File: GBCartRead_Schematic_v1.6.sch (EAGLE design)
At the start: 32 parts, among them IC1 74LS595N, IC2 74LS595N

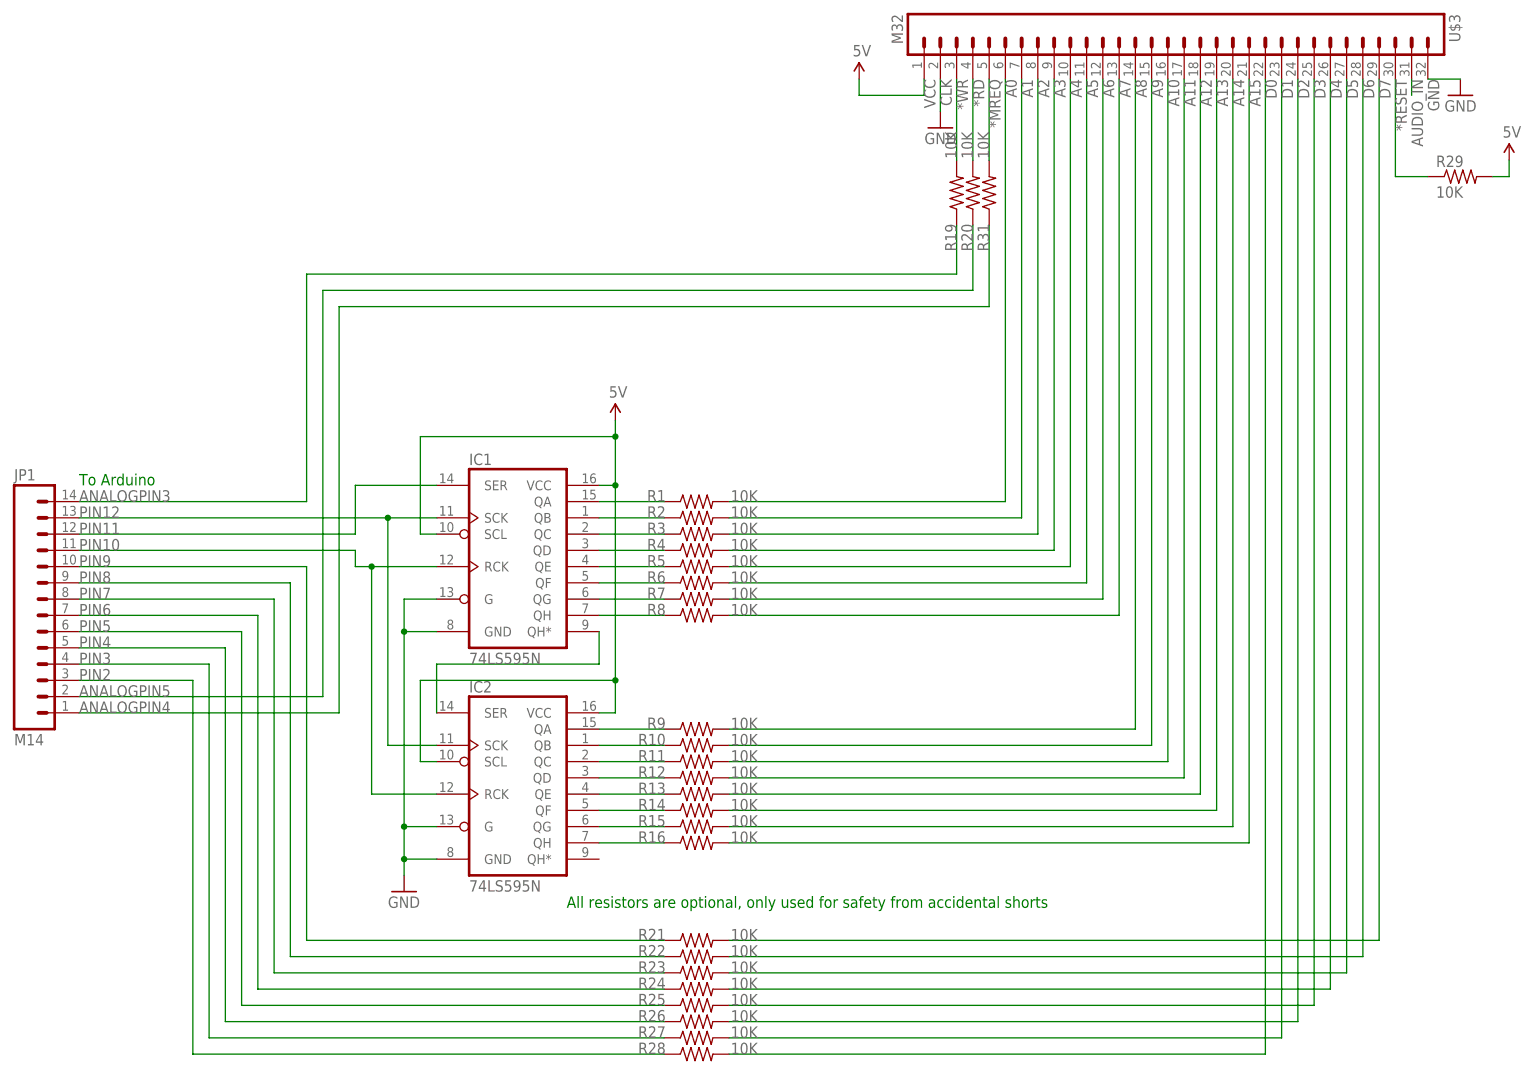
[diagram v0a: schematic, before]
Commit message: v1.6 (3 January 2015) - Speed increase by using a higher baud rate (400Kbit from 57.6Kbit) and using hardware SPI (thanks David R) - Changed SCK from pin 12 to pin 13 for SPI - RAM writing speed increase by continually sending 64bytes data from PC and pausing for 5 ms in-between (Compatible with Gameboy Cart Shield v1.2 if you connect pins 12 and 13 together)
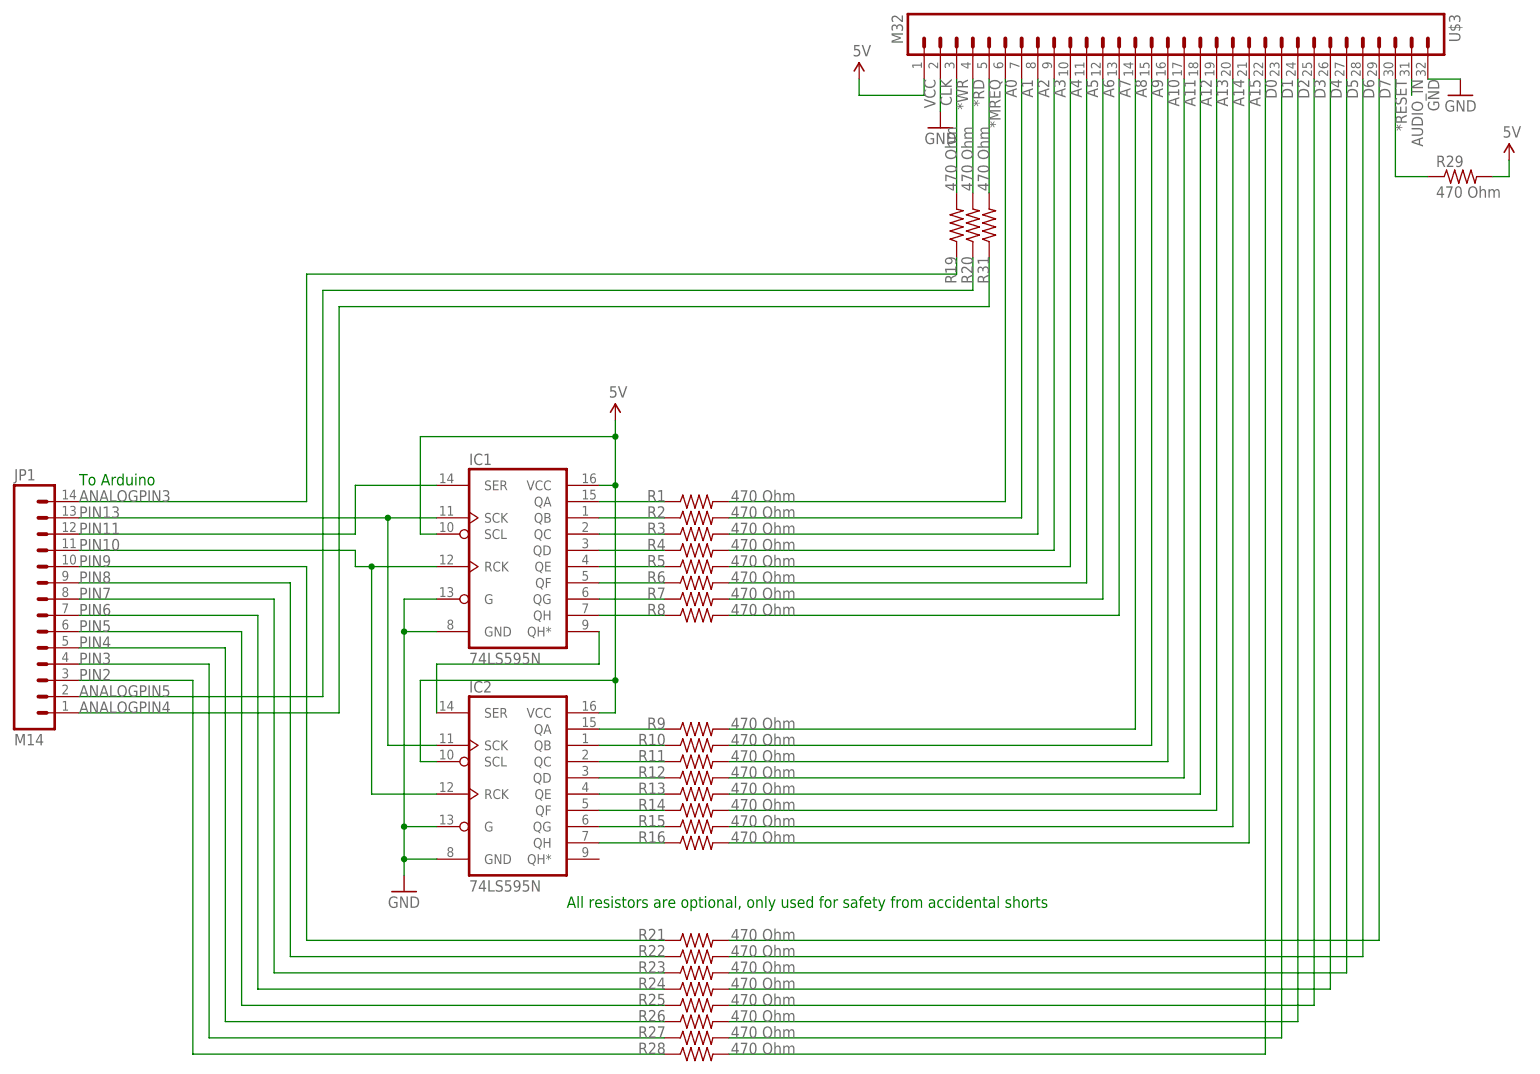
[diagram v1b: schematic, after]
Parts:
- R1, R10, R11, R12, R13, R14, R15, R16, R19, R2, R20, R21, R22, R23, R24, R25, R26, R27, R28, R29, R3, R31, R4, R5, R6, R7, R8, R9: value 10K -> 470 Ohm
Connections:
- net PIN12 renamed PIN13
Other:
- moved on the sheet: R19, R20, R31
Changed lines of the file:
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@@
 <part name="GND2" library="SparkFun" deviceset="GND" device=""/>
 <part name="P+2" library="SparkFun" deviceset="VCC" device="" value="5V"/>
-<part name="R29" library="SparkFun" deviceset="RESISTOR" device="PTH1" value="10K"/>
+<part name="R29" library="SparkFun" deviceset="RESISTOR" device="PTH1" value="470 Ohm"/>
 <part name="U$3" library="SparkFun" deviceset="M32" device=""/>
 <part name="JP1" library="SparkFun" deviceset="M14" device=""/>
-<part name="R19" library="SparkFun" deviceset="RESISTOR" device="PTH1" value="10K"/>
-<part name="R31" library="SparkFun" deviceset="RESISTOR" device="PTH1" value="10K"/>
-<part name="R20" library="SparkFun" deviceset="RESISTOR" device="PTH1" value="10K"/>
-<part name="R1" library="SparkFun" deviceset="RESISTOR" device="PTH1" value="10K"/>
-<part name="R2" library="SparkFun" deviceset="RESISTOR" device="PTH1" value="10K"/>
-<part name="R3" library="SparkFun" deviceset="RESISTOR" device="PTH1" value="10K"/>
-<part name="R4" library="SparkFun" deviceset="RESISTOR" device="PTH1" value="10K"/>
-<part name="R5" library="SparkFun" deviceset="RESISTOR" device="PTH1" value="10K"/>
-<part name="R6" library="SparkFun" deviceset="RESISTOR" device="PTH1" value="10K"/>
-<part name="R7" library="SparkFun" deviceset="RESISTOR" device="PTH1" value="10K"/>
-<part name="R8" library="SparkFun" deviceset="RESISTOR" device="PTH1" value="10K"/>
-<part name="R9" library="SparkFun" deviceset="RESISTOR" device="PTH1" value="10K"/>
-<part name="R10" library="SparkFun" deviceset="RESISTOR" device="PTH1" value="10K"/>
-<part name="R11" library="SparkFun" deviceset="RESISTOR" device="PTH1" value="10K"/>
-<part name="R12" library="SparkFun" deviceset="RESISTOR" device="PTH1" value="10K"/>
-<part name="R13" library="SparkFun" deviceset="RESISTOR" device="PTH1" value="10K"/>
-<part name="R14" library="SparkFun" deviceset="RESISTOR" device="PTH1" value="10K"/>
-<part name="R15" library="SparkFun" deviceset="RESISTOR" device="PTH1" value="10K"/>
-<part name="R16" library="SparkFun" deviceset="RESISTOR" device="PTH1" value="10K"/>
-<part name="R21" library="SparkFun" deviceset="RESISTOR" device="PTH1" value="10K"/>
-<part name="R22" library="SparkFun" deviceset="RESISTOR" device="PTH1" value="10K"/>
-<part name="R23" library="SparkFun" deviceset="RESISTOR" device="PTH1" value="10K"/>
-<part name="R24" library="SparkFun" deviceset="RESISTOR" device="PTH1" value="10K"/>
-<part name="R25" library="SparkFun" deviceset="RESISTOR" device="PTH1" value="10K"/>
-<part name="R26" library="SparkFun" deviceset="RESISTOR" device="PTH1" value="10K"/>
-<part name="R27" library="SparkFun" deviceset="RESISTOR" device="PTH1" value="10K"/>
-<part name="R28" library="SparkFun" deviceset="RESISTOR" device="PTH1" value="10K"/>
+<part name="R19" library="SparkFun" deviceset="RESISTOR" device="PTH1" value="470 Ohm"/>
+<part name="R31" library="SparkFun" deviceset="RESISTOR" device="PTH1" value="470 Ohm"/>
+<part name="R20" library="SparkFun" deviceset="RESISTOR" device="PTH1" value="470 Ohm"/>
+<part name="R1" library="SparkFun" deviceset="RESISTOR" device="PTH1" value="470 Ohm"/>
+<part name="R2" library="SparkFun" deviceset="RESISTOR" device="PTH1" value="470 Ohm"/>
+<part name="R3" library="SparkFun" deviceset="RESISTOR" device="PTH1" value="470 Ohm"/>
+<part name="R4" library="SparkFun" deviceset="RESISTOR" device="PTH1" value="470 Ohm"/>
+<part name="R5" library="SparkFun" deviceset="RESISTOR" device="PTH1" value="470 Ohm"/>
+<part name="R6" library="SparkFun" deviceset="RESISTOR" device="PTH1" value="470 Ohm"/>
+<part name="R7" library="SparkFun" deviceset="RESISTOR" device="PTH1" value="470 Ohm"/>
+<part name="R8" library="SparkFun" deviceset="RESISTOR" device="PTH1" value="470 Ohm"/>
+<part name="R9" library="SparkFun" deviceset="RESISTOR" device="PTH1" value="470 Ohm"/>
+<part name="R10" library="SparkFun" deviceset="RESISTOR" device="PTH1" value="470 Ohm"/>
+<part name="R11" library="SparkFun" deviceset="RESISTOR" device="PTH1" value="470 Ohm"/>
+<part name="R12" library="SparkFun" deviceset="RESISTOR" device="PTH1" value="470 Ohm"/>
+<part name="R13" library="SparkFun" deviceset="RESISTOR" device="PTH1" value="470 Ohm"/>
+<part name="R14" library="SparkFun" deviceset="RESISTOR" device="PTH1" value="470 Ohm"/>
+<part name="R15" library="SparkFun" deviceset="RESISTOR" device="PTH1" value="470 Ohm"/>
+<part name="R16" library="SparkFun" deviceset="RESISTOR" device="PTH1" value="470 Ohm"/>
+<part name="R21" library="SparkFun" deviceset="RESISTOR" device="PTH1" value="470 Ohm"/>
+<part name="R22" library="SparkFun" deviceset="RESISTOR" device="PTH1" value="470 Ohm"/>
+<part name="R23" library="SparkFun" deviceset="RESISTOR" device="PTH1" value="470 Ohm"/>
+<part name="R24" library="SparkFun" deviceset="RESISTOR" device="PTH1" value="470 Ohm"/>
+<part name="R25" library="SparkFun" deviceset="RESISTOR" device="PTH1" value="470 Ohm"/>
+<part name="R26" library="SparkFun" deviceset="RESISTOR" device="PTH1" value="470 Ohm"/>
+<part name="R27" library="SparkFun" deviceset="RESISTOR" device="PTH1" value="470 Ohm"/>
+<part name="R28" library="SparkFun" deviceset="RESISTOR" device="PTH1" value="470 Ohm"/>
 <part name="GND3" library="SparkFun" deviceset="GND" device=""/>
 </parts>
@@
 <instance part="U$3" gate="G$1" x="167.64" y="134.62" rot="R270"/>
 <instance part="JP1" gate="G$1" x="-12.7" y="43.18"/>
-<instance part="R19" gate="G$1" x="134.62" y="106.68" smashed="yes" rot="R90">
-<attribute name="NAME" x="132.8166" y="101.854" size="1.778" layer="95" rot="R270"/>
-<attribute name="VALUE" x="134.62" y="112.014" size="1.778" layer="96" rot="R90"/>
-</instance>
-<instance part="R31" gate="G$1" x="139.7" y="106.68" smashed="yes" rot="R90">
-<attribute name="NAME" x="137.8966" y="101.854" size="1.778" layer="95" rot="R270"/>
-<attribute name="VALUE" x="139.7" y="112.014" size="1.778" layer="96" rot="R90"/>
-</instance>
-<instance part="R20" gate="G$1" x="137.16" y="106.68" smashed="yes" rot="R90">
-<attribute name="NAME" x="135.3566" y="101.854" size="1.778" layer="95" rot="R270"/>
-<attribute name="VALUE" x="137.16" y="112.014" size="1.778" layer="96" rot="R90"/>
+<instance part="R19" gate="G$1" x="134.62" y="101.6" smashed="yes" rot="R90">
+<attribute name="NAME" x="132.8166" y="96.774" size="1.778" layer="95" rot="R270"/>
+<attribute name="VALUE" x="134.62" y="106.934" size="1.778" layer="96" rot="R90"/>
+</instance>
+<instance part="R31" gate="G$1" x="139.7" y="101.6" smashed="yes" rot="R90">
+<attribute name="NAME" x="137.8966" y="96.774" size="1.778" layer="95" rot="R270"/>
+<attribute name="VALUE" x="139.7" y="106.934" size="1.778" layer="96" rot="R90"/>
+</instance>
+<instance part="R20" gate="G$1" x="137.16" y="101.6" smashed="yes" rot="R90">
+<attribute name="NAME" x="135.3566" y="96.774" size="1.778" layer="95" rot="R270"/>
+<attribute name="VALUE" x="137.16" y="106.934" size="1.778" layer="96" rot="R90"/>
 </instance>
 <instance part="R1" gate="G$1" x="93.98" y="58.42" smashed="yes">
@@
 </segment>
 </net>
-<net name="PIN12" class="0">
+<net name="PIN13" class="0">
 <segment>
 <wire x1="53.34" y1="55.88" x2="45.72" y2="55.88" width="0.1524" layer="91"/>
@@
 <wire x1="33.02" y1="93.98" x2="33.02" y2="58.42" width="0.1524" layer="91"/>
 <wire x1="33.02" y1="58.42" x2="-2.54" y2="58.42" width="0.1524" layer="91"/>
-<wire x1="134.62" y1="101.6" x2="134.62" y2="93.98" width="0.1524" layer="91"/>
+<wire x1="134.62" y1="96.52" x2="134.62" y2="93.98" width="0.1524" layer="91"/>
 <wire x1="33.02" y1="93.98" x2="134.62" y2="93.98" width="0.1524" layer="91"/>
 <label x="-2.54" y="58.42" size="1.778" layer="95"/>
@@
 <wire x1="35.56" y1="91.44" x2="35.56" y2="27.94" width="0.1524" layer="91"/>
 <wire x1="35.56" y1="27.94" x2="-2.54" y2="27.94" width="0.1524" layer="91"/>
-<wire x1="137.16" y1="101.6" x2="137.16" y2="91.44" width="0.1524" layer="91"/>
+<wire x1="137.16" y1="96.52" x2="137.16" y2="91.44" width="0.1524" layer="91"/>
 <wire x1="35.56" y1="91.44" x2="137.16" y2="91.44" width="0.1524" layer="91"/>
 <label x="-2.54" y="27.94" size="1.778" layer="95"/>
@@
 <wire x1="38.1" y1="25.4" x2="38.1" y2="88.9" width="0.1524" layer="91"/>
 <wire x1="-2.54" y1="25.4" x2="38.1" y2="25.4" width="0.1524" layer="91"/>
-<wire x1="139.7" y1="101.6" x2="139.7" y2="88.9" width="0.1524" layer="91"/>
+<wire x1="139.7" y1="96.52" x2="139.7" y2="88.9" width="0.1524" layer="91"/>
 <wire x1="38.1" y1="88.9" x2="139.7" y2="88.9" width="0.1524" layer="91"/>
 <label x="-2.54" y="25.4" size="1.778" layer="95"/>
@@
 <net name="*RD" class="0">
 <segment>
-<wire x1="137.16" y1="124.46" x2="137.16" y2="111.76" width="0.1524" layer="91"/>
+<wire x1="137.16" y1="124.46" x2="137.16" y2="106.68" width="0.1524" layer="91"/>
 <label x="137.16" y="124.46" size="1.778" layer="95" rot="R270"/>
 <pinref part="U$3" gate="G$1" pin="4"/>
@@
 <net name="*WR" class="0">
 <segment>
-<wire x1="134.62" y1="124.46" x2="134.62" y2="111.76" width="0.1524" layer="91"/>
+<wire x1="134.62" y1="124.46" x2="134.62" y2="106.68" width="0.1524" layer="91"/>
 <label x="134.62" y="124.46" size="1.778" layer="95" rot="R270"/>
 <pinref part="U$3" gate="G$1" pin="3"/>
@@
 <net name="*MREQ" class="0">
 <segment>
-<wire x1="139.7" y1="124.46" x2="139.7" y2="111.76" width="0.1524" layer="91"/>
+<wire x1="139.7" y1="124.46" x2="139.7" y2="106.68" width="0.1524" layer="91"/>
 <label x="139.7" y="124.46" size="1.778" layer="95" rot="R270"/>
 <pinref part="U$3" gate="G$1" pin="5"/>
